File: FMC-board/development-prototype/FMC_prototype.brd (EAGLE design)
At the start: 103.9 x 69.8 mm, 91 parts, among them J1 PJ-102AH, J2 DC_POWER_JACK-PJ-102AH, U1 TPS79301, U10 ADN4664, U11 ADN4663, U2 TPS79333, U3 ADN4663, U4 ADN4663, U5 ADN4664, U6 PDS1-S12-S5-S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

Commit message: rough layout
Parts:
- moved L1 235.1 mm to (85.6, 14.0)
- moved C11 227.2 mm to (80.8, 13.7)
- moved G22_ISO 218.7 mm to (99.1, 4.83)
- moved R13 198.4 mm to (125.5, 62.5)
- moved C18_DIR 197.3 mm to (4.57, 61.7)
- moved H22_ISO 196.1 mm to (78.7, 4.83)
- moved H21_ISO 191.2 mm to (89.2, 4.83)
- moved D4 191.2 mm to (123.2, 54.4)
- moved R12 182.7 mm to (123.7, 46.0)
- moved D3 182.5 mm to (125.7, 40.4)
- moved C15_DIR 171.8 mm to (4.57, 49.3)
- moved R1 163.4 mm to (102.4, 23.9), turned to 270 degrees
- moved D1 157.2 mm to (96.5, 22.1), turned to 270 degrees
- moved D2 154.3 mm to (100.6, 16.3)
- moved R2 148.4 mm to (95.2, 13.5)
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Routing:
- net MISO1+: track 101.9 -> 59.3 mm, vias 6 -> 4
- net +3V3: track 133.6 -> 93.3 mm
- net MOSI+: track 86.6 -> 51.0 mm, vias 2 -> 1
- net MISO2+: track 80.8 -> 52.1 mm, vias 4 -> 3
- net MISO1-: track 71.8 -> 47.3 mm, vias 4 -> 3
- net SCLK+: track 59.7 -> 42.3 mm, vias 3 -> 1
- net TP3_TO_SMA: track 48.4 -> 31.2 mm
- net TP4: track 22.9 -> 5.94 mm
- net TP1_FROM_SMA: track 57.2 -> 42.2 mm
- net MOSI-: track 51.9 -> 37.0 mm
- net GND: track 69.7 -> 54.9 mm, vias 10 -> 9
- net SCLK-: track 65.2 -> 50.8 mm
- net CS+: track 63.5 -> 49.3 mm, vias 3 -> 1
- net CS-: track 66.7 -> 52.6 mm
- net MISO2-: track 64.1 -> 50.7 mm
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
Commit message: more layout
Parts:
- moved R13 74.2 mm to (51.3, 60.7)
- moved D4 73.2 mm to (50.5, 63.2)
- moved R12 72.7 mm to (54.6, 23.4)
- moved D3 69.7 mm to (58.2, 23.4), turned to 270 degrees
- moved U8 38.7 mm to (47.2, 62.2), turned to 180 degrees
- moved R14 21.7 mm to (18.3, 34.3), turned to 0 degrees
- moved R17 20.2 mm to (18.3, 29.0), turned to 0 degrees
- moved R15 19.8 mm to (18.3, 32.5), turned to 0 degrees
- moved R16 18.1 mm to (18.3, 30.7), turned to 0 degrees
- moved R18 17.5 mm to (18.3, 27.2), turned to 0 degrees
- moved R23 16.9 mm to (18.3, 18.0), turned to 0 degrees
- moved R22 15.8 mm to (18.3, 20.1), turned to 0 degrees
- moved R19 14.0 mm to (18.3, 25.4), turned to 0 degrees
- moved R21 12.1 mm to (18.3, 21.8), turned to 0 degrees
- moved R20 11.6 mm to (18.3, 23.6), turned to 0 degrees
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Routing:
- net GND: track 54.9 -> 119.5 mm, vias 9 -> 10
- net MISO2+: track 52.1 -> 0.00 mm, vias 3 -> 0
- net MISO2-: track 50.7 -> 0.00 mm, vias 3 -> 0
- net CS-: track 52.6 -> 4.47 mm
- net MISO1-: track 47.3 -> 0.00 mm, vias 3 -> 0
- net A_CS-: track 0.00 -> 46.3 mm, vias 0 -> 2
- net SCLK-: track 50.8 -> 5.59 mm
- net A_CS+: track 0.00 -> 43.6 mm
- net A_SCLK+: track 0.00 -> 43.5 mm, vias 0 -> 2
- net CS+: track 49.3 -> 6.20 mm
- net MISO1+: track 59.3 -> 17.5 mm, vias 4 -> 1
- net A_SCLK-: track 0.00 -> 41.5 mm
- net A_MOSI+: track 0.00 -> 38.4 mm, vias 0 -> 2
- net MOSI-: track 37.0 -> 0.00 mm, vias 1 -> 0
- net +3V3: track 93.3 -> 130.3 mm, vias 3 -> 4
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
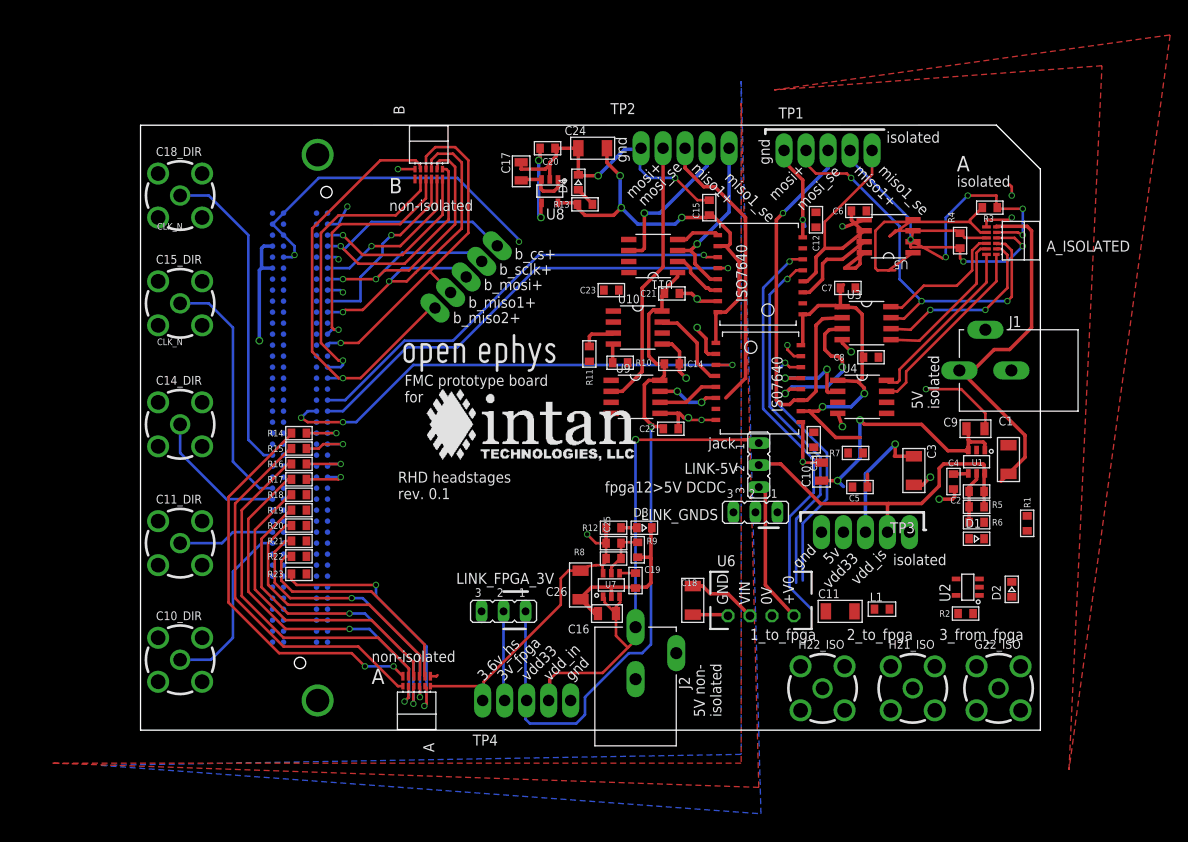
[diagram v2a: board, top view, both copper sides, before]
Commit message: layout mostly cleaned up now
still needs proper DRC, probably ERC and almost all labels etc need to
be fixed
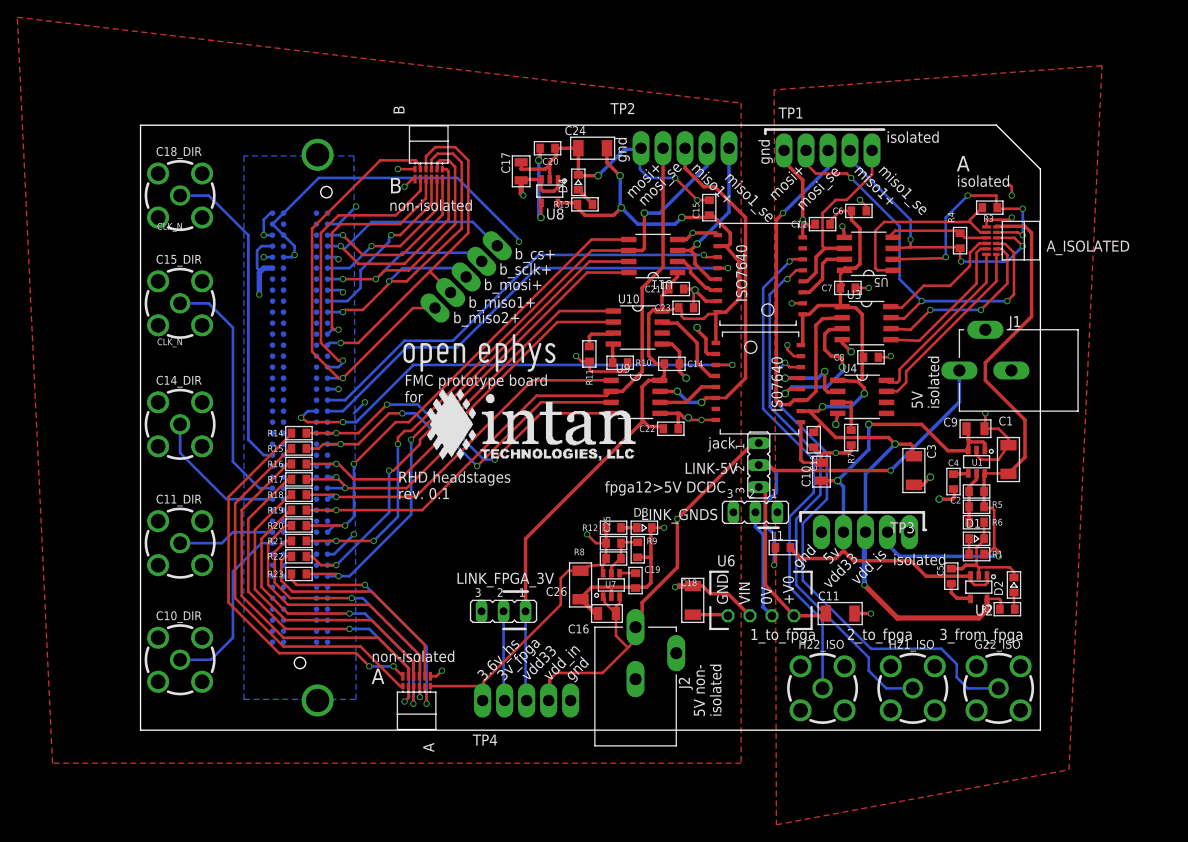
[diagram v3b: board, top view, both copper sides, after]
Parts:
- moved C5 14.7 mm to (93.6, 17.8), turned to 90 degrees
- moved L1 13.5 mm to (74.2, 21.1)
- moved C23 8.87 mm to (63.0, 48.8)
- moved R1 6.84 mm to (96.5, 20.3), turned to 180 degrees
- moved R2 4.85 mm to (100.1, 14.0)
- moved U5 3.06 mm to (84.1, 55.0)
- moved R7 1.85 mm to (82.0, 33.8), turned to 90 degrees
- moved U2 1.27 mm to (96.8, 16.5), turned to 180 degrees
- moved C12 0.92 mm to (78.7, 58.4), turned to 0 degrees
- moved C21 0.72 mm to (61.8, 50.9)
- moved D2 0.57 mm to (100.8, 16.8)
- moved C11 0.25 mm to (80.8, 13.5)
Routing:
- net MISO2+: track 0.00 -> 58.7 mm, vias 0 -> 2
- net MISO1+: track 17.5 -> 75.1 mm, vias 1 -> 4
- net MISO1-: track 0.00 -> 56.8 mm, vias 0 -> 2
- net MISO2-: track 0.00 -> 55.8 mm, vias 0 -> 2
- net GND_ISO: track 48.8 -> 103.7 mm, vias 11 -> 16
- net 12V_FPGA: track 56.0 -> 105.6 mm, vias 1 -> 2
- net +5V0_EXT: track 0.00 -> 46.5 mm, vias 0 -> 2
- net MOSI-: track 0.00 -> 42.0 mm, vias 0 -> 1
- net MOSI+: track 31.3 -> 73.2 mm, vias 0 -> 1
- net GND: track 119.5 -> 160.7 mm, vias 10 -> 22
- net CS-: track 4.47 -> 43.3 mm, vias 1 -> 3
- net CS+: track 6.20 -> 44.9 mm, vias 1 -> 3
- net SCLK+: track 5.59 -> 43.5 mm, vias 1 -> 3
- net SCLK-: track 5.59 -> 42.3 mm, vias 1 -> 3
- net +3V3_ISO: track 67.4 -> 102.1 mm, vias 3 -> 4
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
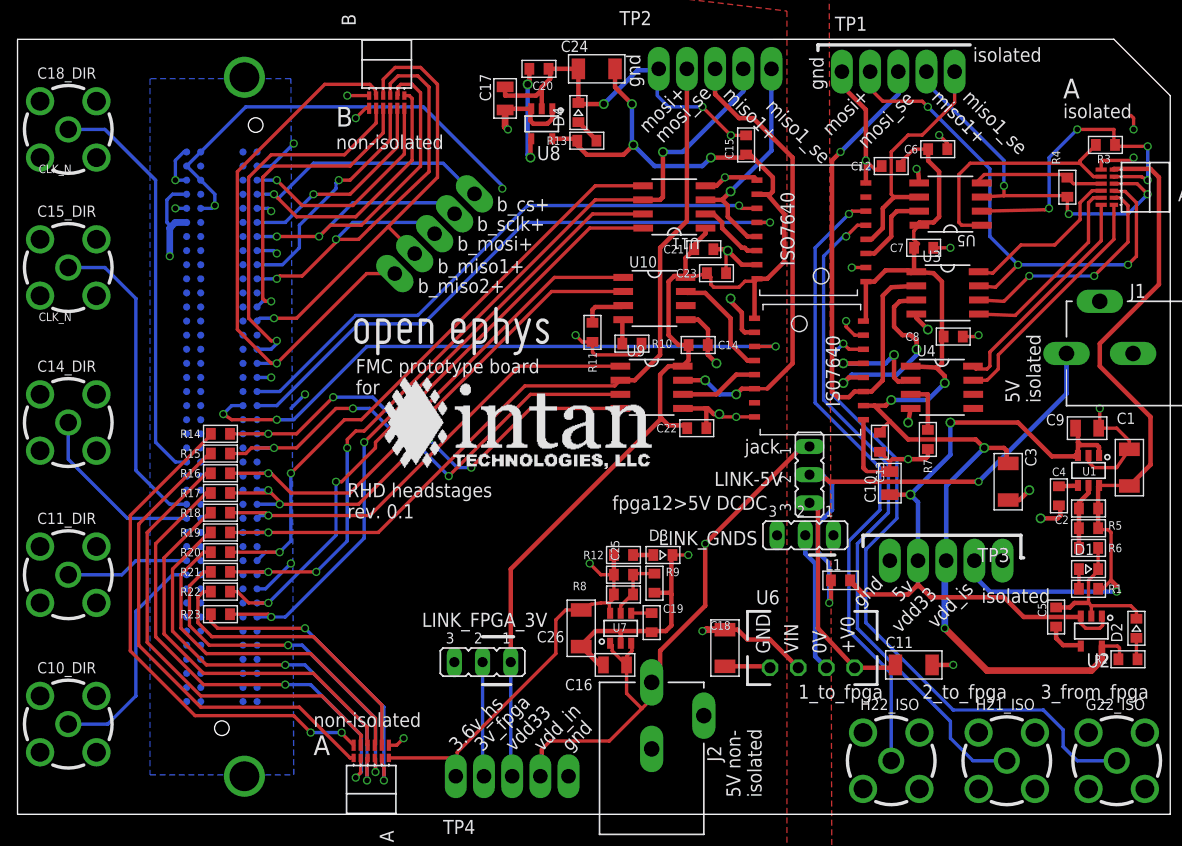
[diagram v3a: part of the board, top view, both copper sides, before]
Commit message: small layout fixes
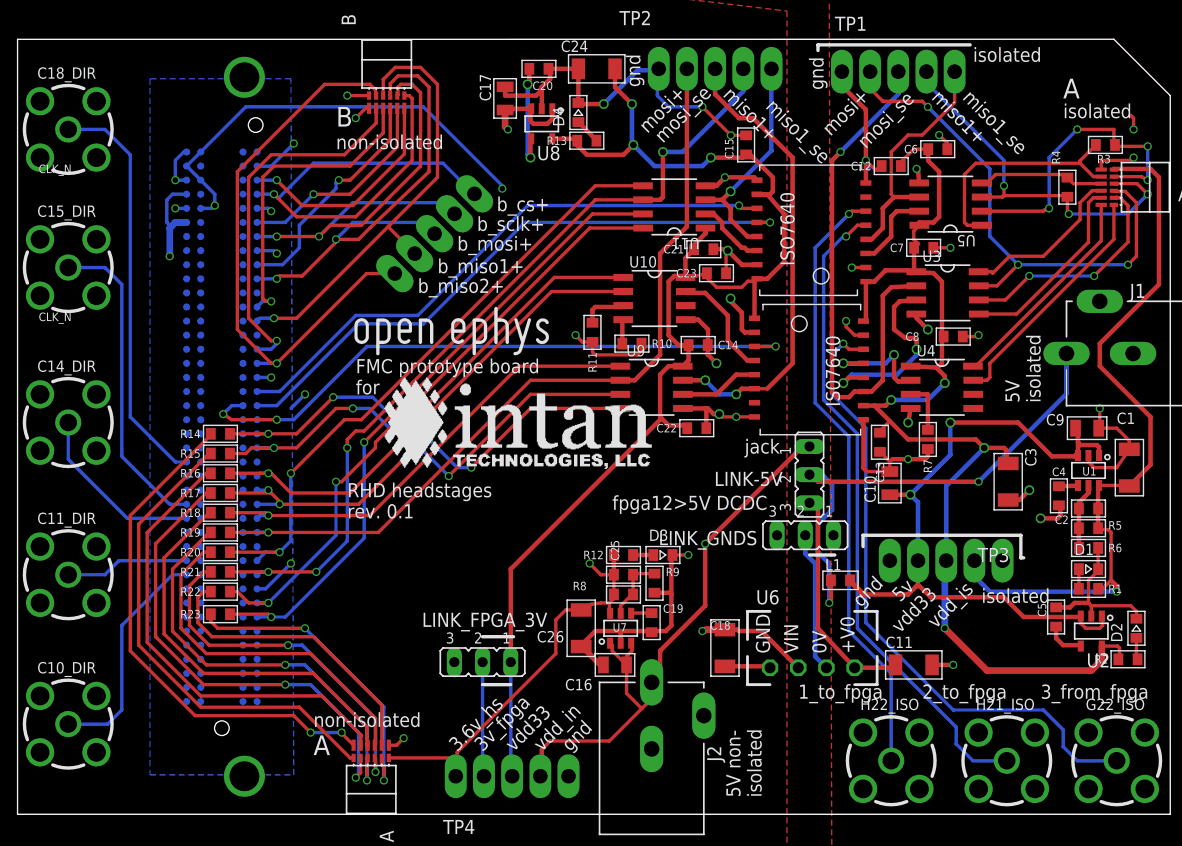
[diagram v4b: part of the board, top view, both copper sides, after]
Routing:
- net TP3_TO_SMA: track 59.8 -> 57.5 mm
- net TP1_FROM_SMA: track 61.7 -> 59.4 mm
- net TP2_FROM_SMA: track 57.3 -> 55.0 mm
- net MISO2-_ISOLATED: track 22.7 -> 21.7 mm
- net CS-_ISOLATED: track 20.4 -> 19.5 mm
- net MISO1-_ISOLATED: track 12.2 -> 11.3 mm

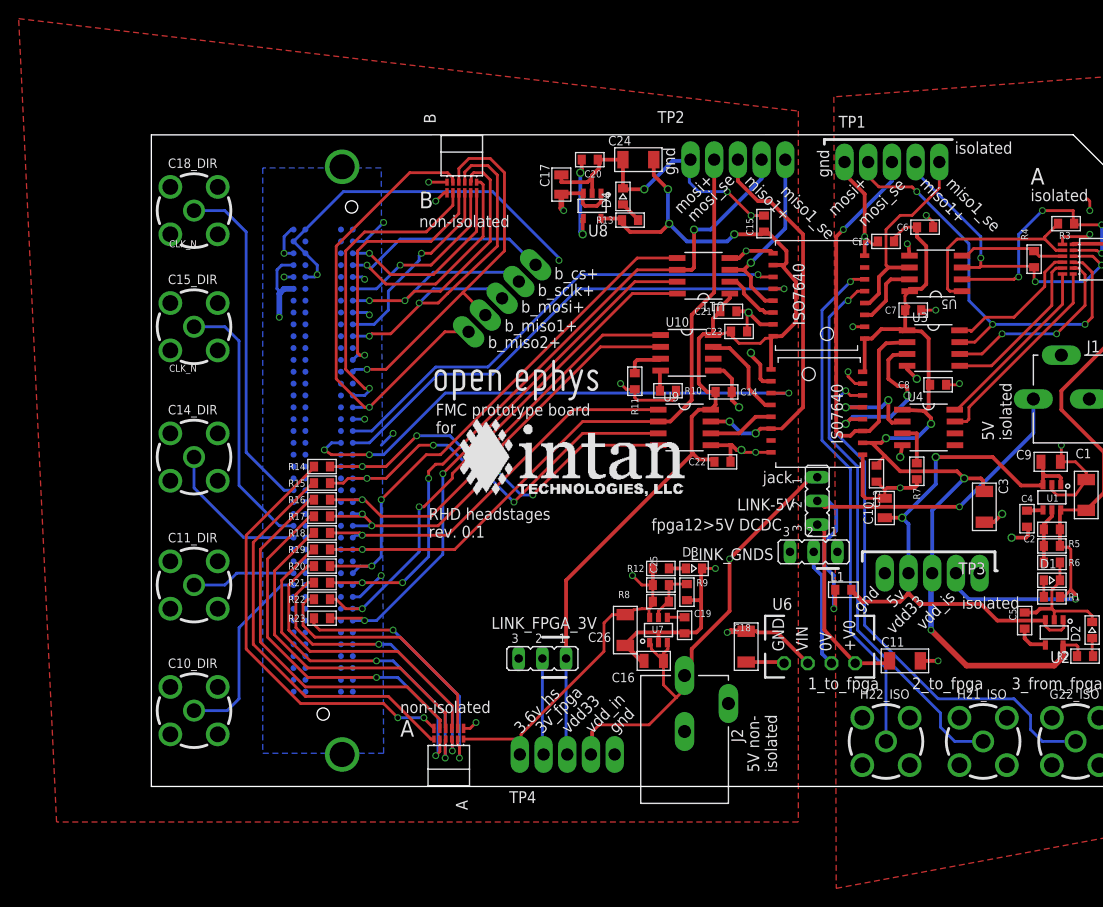
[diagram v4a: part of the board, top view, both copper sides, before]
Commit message: improved B headstage routing
no more branches going to test points
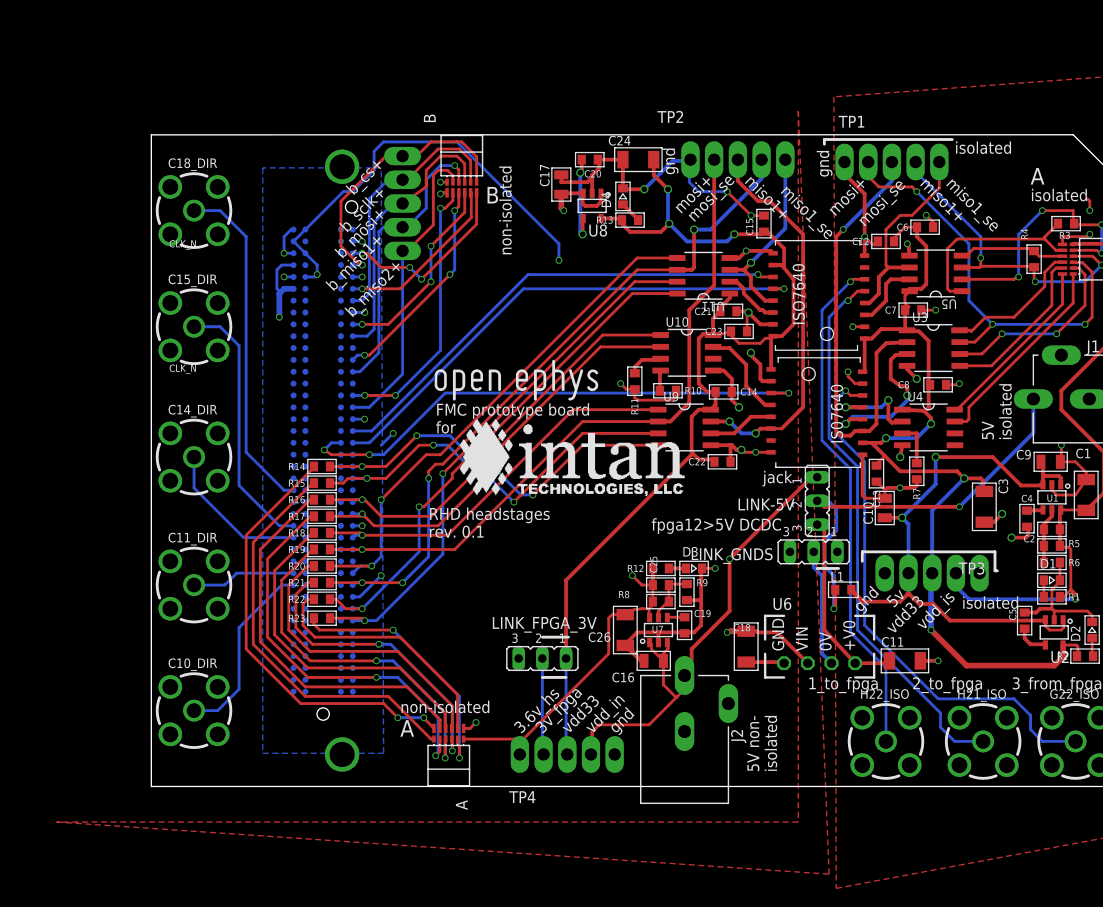
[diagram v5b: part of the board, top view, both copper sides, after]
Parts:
- moved TP5 14.7 mm to (26.9, 62.5), turned to 90 degrees
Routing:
- net B_MISO2+: track 51.3 -> 33.0 mm, vias 1 -> 0
- net B_CS+: track 44.0 -> 29.5 mm
- net B_SCLK+: track 41.1 -> 28.1 mm, vias 2 -> 0
- net B_MOSI+: track 42.4 -> 29.9 mm, vias 2 -> 0
- net B_MISO1+: track 40.9 -> 31.4 mm
- net 3V_FPGA: track 96.1 -> 101.4 mm
- net B_MISO1-: track 28.0 -> 23.4 mm, vias 1 -> 3
- net B_MISO2-: track 33.2 -> 29.1 mm, vias 1 -> 3
- net GND: track 160.7 -> 157.0 mm
- net +3V6: track 96.1 -> 93.1 mm
- net 12V_FPGA: track 105.6 -> 103.7 mm
- net VDD_IN: track 108.4 -> 107.2 mm
- net TP4: track 20.7 -> 20.1 mm
- net SCLK_ISOLATED_SE: track 17.6 -> 17.1 mm
- net B_MOSI-: track 21.0 -> 21.3 mm, vias 1 -> 3
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
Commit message: small cleanups
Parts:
- moved U$16 1.80 mm to (31.2, 29.2)
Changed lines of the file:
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@@
 <grid distance="0.01" unitdist="inch" unit="inch" style="lines" multiple="1" display="yes" altdistance="0.0125" altunitdist="inch" altunit="inch"/>
 <layers>
-<layer number="1" name="Top" color="4" fill="1" visible="no" active="yes"/>
+<layer number="1" name="Top" color="4" fill="1" visible="yes" active="yes"/>
 <layer number="2" name="$GND" color="2" fill="1" visible="no" active="yes"/>
 <layer number="3" name="Route3" color="4" fill="3" visible="no" active="no"/>
@@
 <layer number="13" name="Route13" color="4" fill="5" visible="no" active="no"/>
 <layer number="14" name="Route14" color="1" fill="6" visible="no" active="no"/>
-<layer number="15" name="$VCC" color="3" fill="1" visible="yes" active="yes"/>
+<layer number="15" name="$VCC" color="3" fill="1" visible="no" active="yes"/>
 <layer number="16" name="Bottom" color="1" fill="1" visible="no" active="yes"/>
 <layer number="17" name="Pads" color="2" fill="1" visible="yes" active="yes"/>
@@
 <text x="41.91" y="5.588" size="1.27" layer="25" font="vector" ratio="15" rot="R45">3v_fpga</text>
 <text x="39.624" y="5.588" size="1.27" layer="25" font="vector" ratio="15" rot="R45">3.6v_hs</text>
-<text x="29.718" y="26.67" size="1.27" layer="25" font="vector" ratio="15">RHD headstages
+<text x="30.734" y="25.908" size="1.27" layer="25" font="vector" ratio="15">RHD headstages
 rev. 0.1</text>
 <text x="26.162" y="56.642" size="1.27" layer="25" font="vector" ratio="15" rot="R225">b_miso2+</text>
@@
 <attribute name="VALUE" x="58.166" y="17.526" size="0.762" layer="27" font="vector" ratio="10" align="center-left"/>
 </element>
-<element name="U$16" library="RHD2000_eval_board" package="INTAN_LOGO" value="" x="32.512" y="30.48"/>
+<element name="U$16" library="RHD2000_eval_board" package="INTAN_LOGO" value="" x="31.242" y="29.21"/>
 <element name="TP5" library="testpad" package="P5-25-13" value="TP5P5-25-13" x="26.924" y="62.484" smashed="yes" rot="R90">
 <attribute name="TP_SIGNAL_NAME" value="" x="30.734" y="56.768996875" size="1" layer="37" rot="R90"/>
@@
 <vertex x="69.342" y="-3.81"/>
 <vertex x="-10.16" y="-3.81"/>
-<vertex x="72.644" y="-9.398"/>
+<vertex x="-13.716" y="78.486"/>
 </polygon>
 <wire x1="62.2046" y1="42.291" x2="62.2046" y2="41.4274" width="0.4064" layer="1"/>
@@
 <wire x1="31.6865" y1="64.77" x2="30.988" y2="64.77" width="0.3048" layer="1"/>
 <via x="30.988" y="64.77" extent="1-16" drill="0.5"/>
-<wire x1="30.988" y1="64.77" x2="29.845" y2="64.897" width="0" layer="19" extent="1-16"/>
 <wire x1="38.1" y1="64.77" x2="30.988" y2="64.77" width="0.6096" layer="15"/>
 <contactref element="R12" pad="1"/>
